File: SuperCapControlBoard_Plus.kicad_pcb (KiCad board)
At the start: 4 copper layers, 75 x 45 mm, 194 parts, among them J1 MMCX-KWE, J2 MMCX-KWE, J3 MX1.25-2PIN, J4 GH1.25-2PIN, J5 GH1.25-4PIN, J6 ZH1.5_4PIN, J7 ZH1.5_4PIN, Q1 DTC143ZCA, Q2 AGM60P100A, Q3 IRFH7440, Q4 IRFH7440, SW1 TS-1086EV-16, SW2 DIP-1PIN-TH, U1 USBLC6-2SC6, U10 RT9193, U11 74LVC1G32, U12 74LVC1G08, U13 LM5109, U2 INA193, U3 TLV9061, U4 TCAN1044, U5 USBLC6-2SC6, U6 USBLC6-2SC6, U7 STM32G431CxTx, U8 MP2456, U9 MP2456, Y1 25M

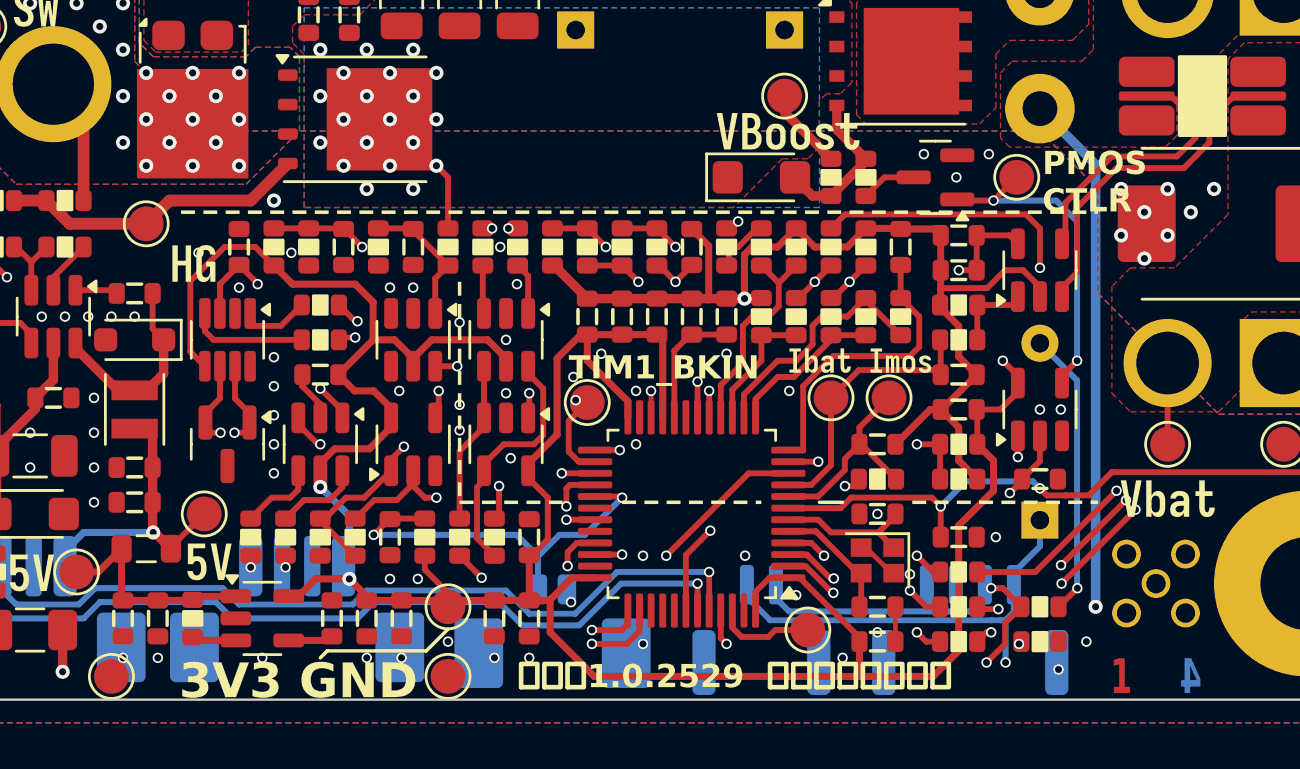
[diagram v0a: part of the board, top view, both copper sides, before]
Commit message: 添加GERBER文件，更正PCB版本丝印为2605
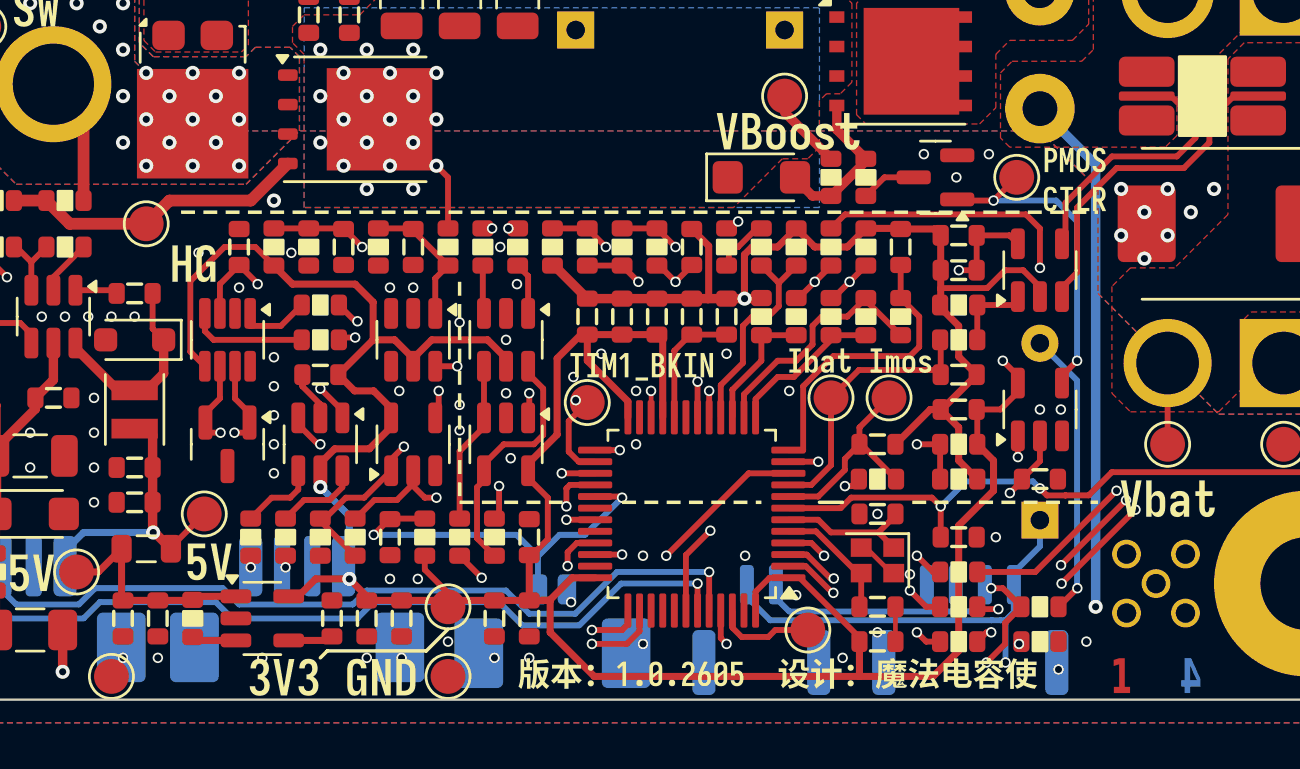
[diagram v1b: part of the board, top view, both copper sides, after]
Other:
- board text removed: "3V3 GND"
- board text removed: "PMOS CTLR"
- board text removed: "TIM1_BKIN"
- board text removed: "版本：1.0.2529 设计：魔法电容使"

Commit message: ``` docs(README): 更新技术文档说明并修正描述错误
- 将全差分放大器重要性说明加粗强调
- 修正下管续流采样误差问题的描述，澄清软件限制措施
- 调整保险丝熔断检测章节标题层级
- 修正PMOS与PWM时序延迟保护章节标题层级
- 优化电源远端电压补偿参考链接格式
- 在STM32引脚说明中明确BOOM_IN引脚标识

chore(kicad): 添加PCB用户注释并调整图层设置

- 在PCB中添加关于LED安装方式的用户注释
- 调整KiCad项目文件的活动图层设置
```
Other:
- board text added: "这个LED是侧贴的 （不知道为什么好多人都喜欢立着贴？？？ 要是立贴我用普通的LED不好吗）"
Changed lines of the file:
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@@
+		)
+	)
+	(gr_text "这个LED是侧贴的\n（不知道为什么好多人都喜欢立着贴？？？\n要是立贴我用普通的LED不好吗）\n"
+		(at 192.288 105.933 0)
+		(layer "Cmts.User")
+		(effects
+			(font
+				(size 2 2)
+				(thickness 0.3)
+				(bold yes)
+			)
+			(justify left bottom)
 		)
 	)
